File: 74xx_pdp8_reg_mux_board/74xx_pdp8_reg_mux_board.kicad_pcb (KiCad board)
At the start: 4 copper layers, 137.2 x 88.9 mm, 42 parts, among them P1 DIL24, P10 DIL6, P11 DIL6, P12 DIL6, P13 DIL6, P2 DIL6, P3 DIL24, P4 DIL6, P5 DIL6, P6 DIL24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

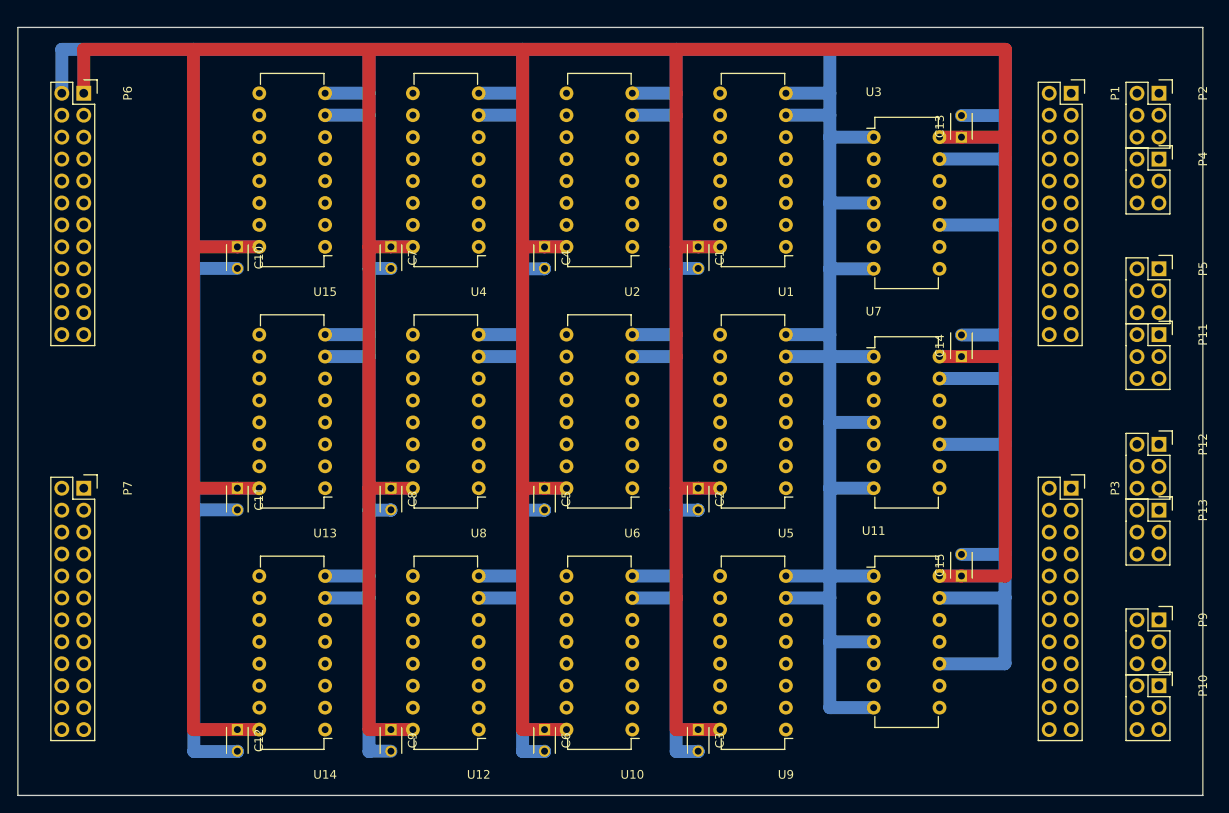
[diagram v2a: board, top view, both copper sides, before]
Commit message: Big changes - elected to switch to board interconnections along one long edge only. Boards to connect to backplane via right-angled DIL connectors. Both register boards and register mux boards thusly modified.
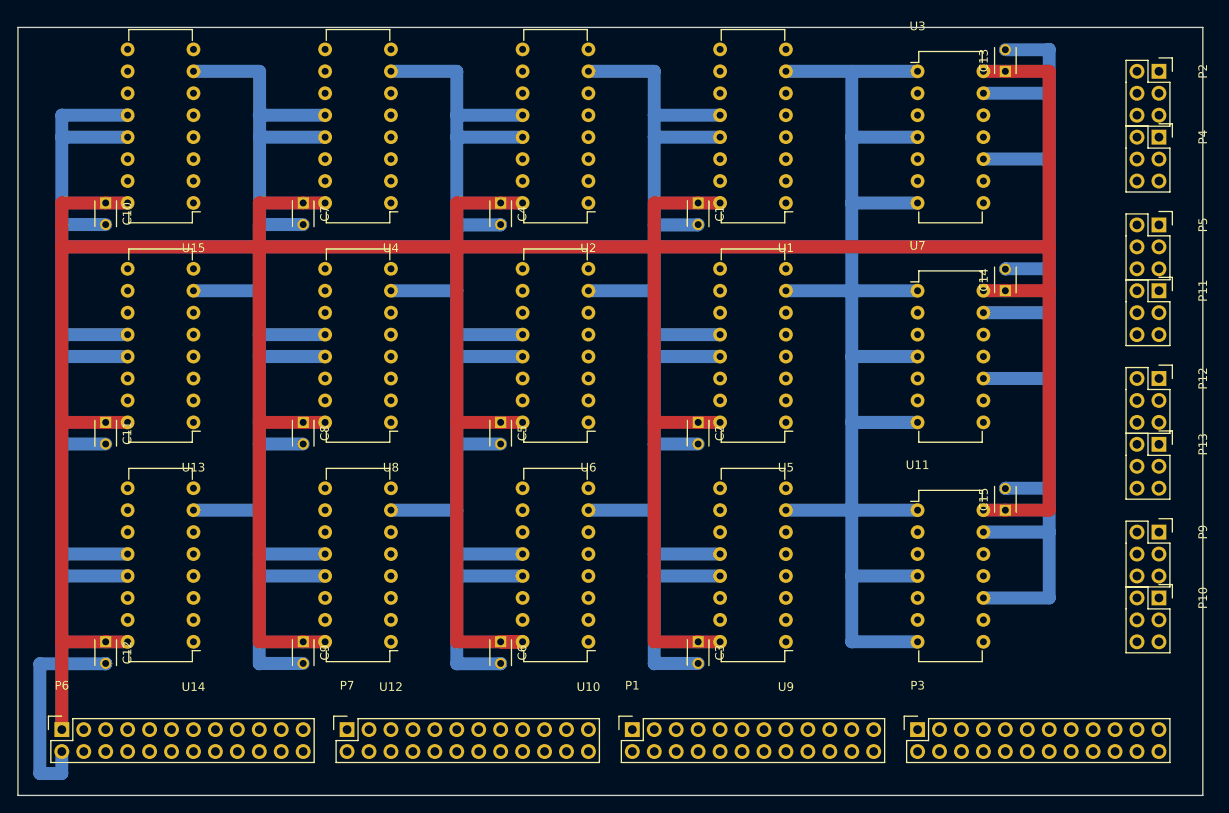
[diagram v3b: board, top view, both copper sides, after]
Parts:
- moved P1 89.5 mm to (101.6, 106.7), turned to 0 degrees
- moved P6 73.7 mm to (35.6, 106.7), turned to 0 degrees
- moved P7 41.3 mm to (68.6, 106.7), turned to 0 degrees
- moved P3 33.1 mm to (134.6, 106.7), turned to 0 degrees
- moved U14 18.3 mm to (50.8, 96.5)
- moved C12 18.3 mm to (40.6, 96.5)
- moved U13 17.0 mm to (50.8, 71.1)
- moved C11 17.0 mm to (40.6, 71.1)
- moved U15 16.1 mm to (50.8, 45.7)
- moved C10 16.1 mm to (40.6, 45.7)
- moved C9 14.4 mm to (63.5, 96.5)
- moved U12 14.4 mm to (73.7, 96.5)
- moved C8 12.7 mm to (63.5, 71.1)
- moved U8 12.7 mm to (73.7, 71.1)
- moved C6 11.4 mm to (86.4, 96.5)
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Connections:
- U1 pad 12: (no net) -> GND
- U1 pad 13: (no net) -> GND
- U1 pad 8: GND -> (no net)
- U10 pad 12: (no net) -> GND
- U10 pad 13: (no net) -> GND
- U10 pad 8: GND -> (no net)
- U12 pad 12: (no net) -> GND
- U12 pad 13: (no net) -> GND
- U12 pad 8: GND -> (no net)
- U13 pad 12: (no net) -> GND
- U13 pad 13: (no net) -> GND
- U13 pad 8: GND -> (no net)
- U14 pad 12: (no net) -> GND
- U14 pad 13: (no net) -> GND
- U14 pad 8: GND -> (no net)
- U15 pad 12: (no net) -> GND
- U15 pad 13: (no net) -> GND
- U15 pad 8: GND -> (no net)
- U2 pad 12: (no net) -> GND
- U2 pad 13: (no net) -> GND
- U2 pad 8: GND -> (no net)
- U4 pad 12: (no net) -> GND
- U4 pad 13: (no net) -> GND
- U4 pad 8: GND -> (no net)
- U5 pad 12: (no net) -> GND
- U5 pad 13: (no net) -> GND
- U5 pad 8: GND -> (no net)
- U6 pad 12: (no net) -> GND
- U6 pad 13: (no net) -> GND
- U6 pad 8: GND -> (no net)
- U8 pad 12: (no net) -> GND
- U8 pad 13: (no net) -> GND
- U8 pad 8: GND -> (no net)
- U9 pad 12: (no net) -> GND
- U9 pad 13: (no net) -> GND
- U9 pad 8: GND -> (no net)
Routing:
- net GND: track 853.7 -> 998.6 mm
- net VCC: track 579.1 -> 497.8 mm
